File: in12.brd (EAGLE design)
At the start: 146.1 x 33.7 mm, 32 parts, among them J1 1-2328702-0

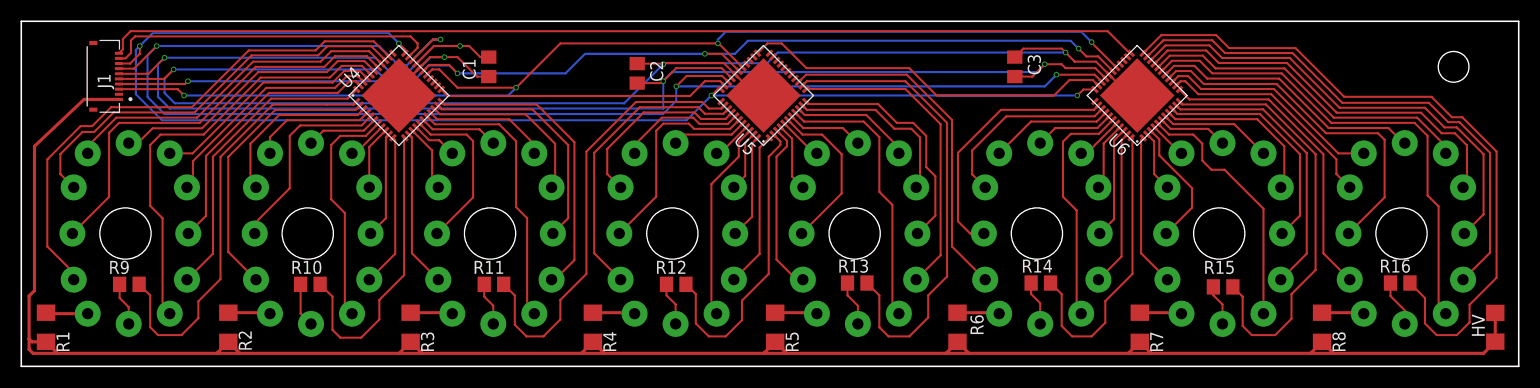
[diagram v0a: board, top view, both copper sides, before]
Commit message: started ratsnest, finished usb-c viring
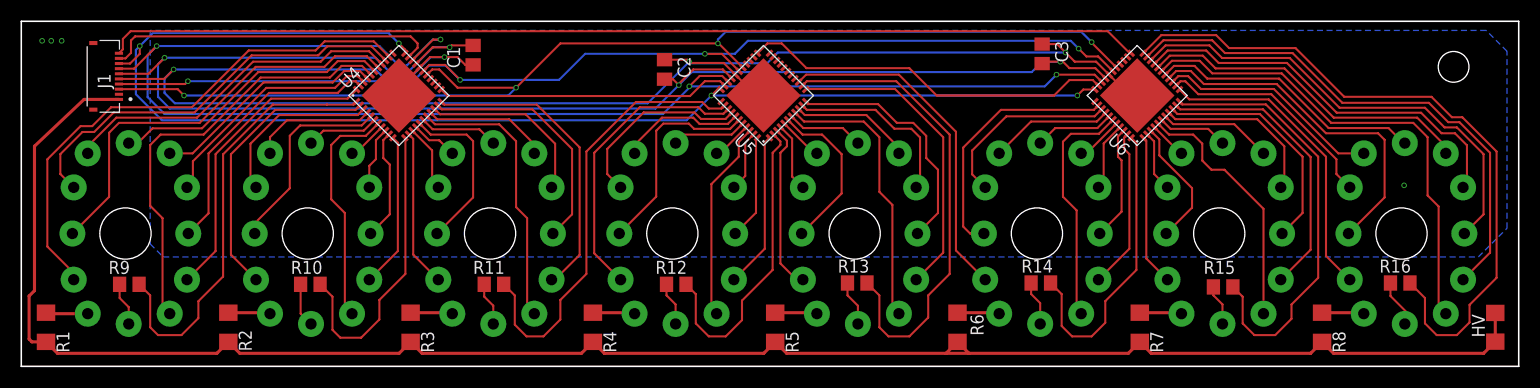
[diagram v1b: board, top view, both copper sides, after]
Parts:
- moved C3 2.95 mm to (99.6, 30.5)
- moved C2 2.69 mm to (62.7, 29.0)
- moved C1 1.91 mm to (44.1, 30.4)
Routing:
- net HV: track 202.0 -> 184.6 mm
- net 3V3: track 158.4 -> 150.2 mm
- net GND: track 165.5 -> 158.2 mm, vias 4 -> 8
- net LE: track 145.4 -> 143.4 mm
- net CLK: track 108.6 -> 109.7 mm
- net L23: track 10.5 -> 11.0 mm
- added copper zone on layer 16, net GND
